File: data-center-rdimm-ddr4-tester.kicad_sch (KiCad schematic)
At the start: 13 parts, among them M1 1296.2013

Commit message: Exclude virtual components from bom
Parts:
- MP1, MP2, MP3, MP4, N1, N2: now left out of the parts list
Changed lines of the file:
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@@
   )
   (symbol (lib_id "data-center-rdimm-ddr4-tester:antmicro_logo") (at 165.735 281.305 0) (unit 1)
-    (in_bom yes) (on_board yes)
+    (in_bom no) (on_board yes)
     (property "Reference" "N2" (id 0) (at 171.1706 278.9428 0)
       (effects (font (size 1.27 1.27)) (justify left))
@@
   )
   (symbol (lib_id "data-center-rdimm-ddr4-tester:oshw_logo") (at 166.37 273.685 0) (unit 1)
-    (in_bom yes) (on_board yes)
+    (in_bom no) (on_board yes)
     (property "Reference" "N1" (id 0) (at 171.2976 273.6088 0)
       (effects (font (size 1.27 1.27)) (justify left))
@@
   )
   (symbol (lib_id "data-center-rdimm-ddr4-tester:PCB_Mount_Hole_3_NPTH") (at 88.9 279.4 0) (unit 1)
-    (in_bom yes) (on_board yes) (fields_autoplaced)
+    (in_bom no) (on_board yes) (fields_autoplaced)
     (property "Reference" "MP2" (id 0) (at 94.107 278.5653 0)
       (effects (font (size 1.27 1.27)) (justify left))
@@
   )
   (symbol (lib_id "data-center-rdimm-ddr4-tester:PCB_Mount_Hole_3_NPTH") (at 88.9 266.7 0) (unit 1)
-    (in_bom yes) (on_board yes) (fields_autoplaced)
+    (in_bom no) (on_board yes) (fields_autoplaced)
     (property "Reference" "MP1" (id 0) (at 94.107 265.8653 0)
       (effects (font (size 1.27 1.27)) (justify left))
@@
   )
   (symbol (lib_id "data-center-rdimm-ddr4-tester:PCB_Mount_Hole_3_NPTH") (at 127 279.4 0) (unit 1)
-    (in_bom yes) (on_board yes) (fields_autoplaced)
+    (in_bom no) (on_board yes) (fields_autoplaced)
     (property "Reference" "MP4" (id 0) (at 132.207 278.5653 0)
       (effects (font (size 1.27 1.27)) (justify left))
@@
   )
   (symbol (lib_id "data-center-rdimm-ddr4-tester:PCB_Mount_Hole_3_NPTH") (at 127 266.7 0) (unit 1)
-    (in_bom yes) (on_board yes) (fields_autoplaced)
+    (in_bom no) (on_board yes) (fields_autoplaced)
     (property "Reference" "MP3" (id 0) (at 132.207 265.8653 0)
       (effects (font (size 1.27 1.27)) (justify left))

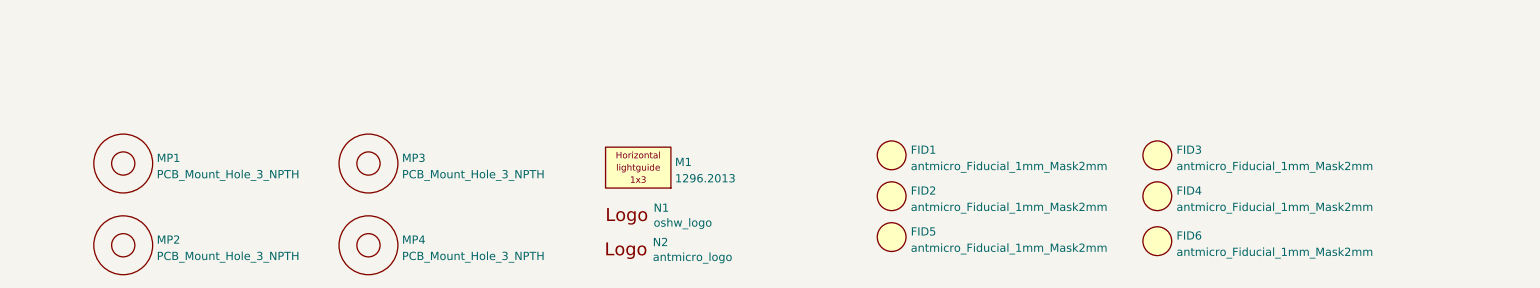
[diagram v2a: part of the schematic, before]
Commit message: Introduce component standardization
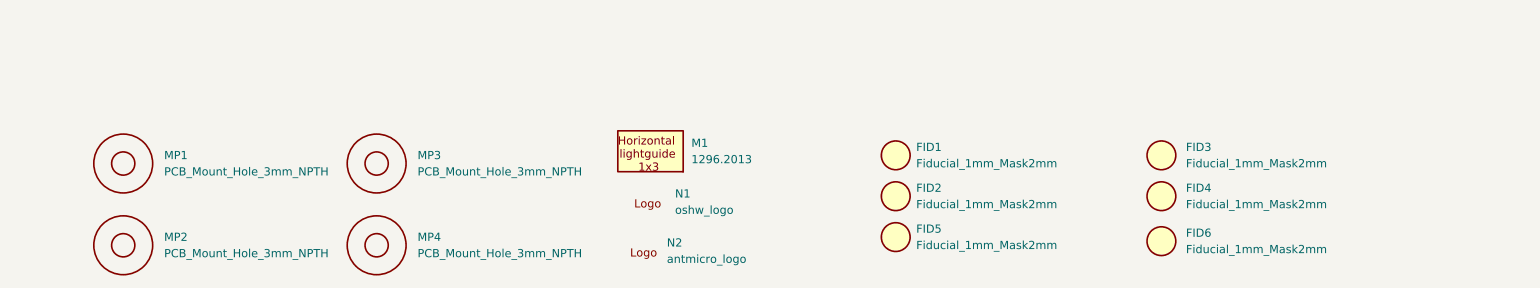
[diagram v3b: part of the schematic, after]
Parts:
- FID1, FID2, FID3, FID4, FID5, FID6: value antmicro_Fiducial_1mm_Mask2mm -> Fiducial_1mm_Mask2mm; symbol data-center-rdimm-ddr4-tester:antmicro_Fiducial_1mm_Mask2mm -> data-center-rdimm-ddr4-tester:Fiducial_1mm_Mask2mm; Author (none) -> Antmicro; License (none) -> Apache-2.0
- M1: value 1296.2013 -> Mech_Lightpipe_Mentor_1296.2013; footprint data-center-rdimm-ddr4-tester-footprints:Mentor_1296.2013 -> data-center-rdimm-ddr4-tester-footprints:Mech_Lightpipe_Mentor_1296.2013; symbol data-center-rdimm-ddr4-tester:1296.2013 -> data-center-rdimm-ddr4-tester:Mech_Lightpipe_Mentor_1296.2013; Author (none) -> Antmicro; License (none) -> Apache-2.0
- MP1, MP2, MP3, MP4: value PCB_Mount_Hole_3_NPTH -> PCB_Mount_Hole_3mm_NPTH; symbol data-center-rdimm-ddr4-tester:PCB_Mount_Hole_3_NPTH -> data-center-rdimm-ddr4-tester:PCB_Mount_Hole_3mm_NPTH; Author (none) -> Antmicro; License (none) -> Apache-2.0; now in the parts list
- N1: footprint data-center-rdimm-ddr4-tester-footprints:OSHW-Logo_5.7x6mm_Mask -> data-center-rdimm-ddr4-tester-footprints:oshw-logo; Author (none) -> Antmicro; License (none) -> Apache-2.0; now in the parts list
- N2: Author (none) -> Antmicro; License (none) -> Apache-2.0; now in the parts list
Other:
- moved on the sheet: FID1, FID2, FID3, FID4, FID5, FID6, M1, MP3, MP4, N1, N2

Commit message: [#55119] component update
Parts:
- FID1, FID2, FID3, FID4, FID5, FID6: footprint data-center-rdimm-ddr4-tester-footprints:Fiducial_1mm_Mask2mm -> antmicro-footprints:Fiducial_1mm_Mask2mm; symbol data-center-rdimm-ddr4-tester:Fiducial_1mm_Mask2mm -> antmicroFiducialMarks:Fiducial_1mm_Mask2mm
- N1: footprint data-center-rdimm-ddr4-tester-footprints:oshw-logo -> antmicro-footprints:oshw-logo; symbol data-center-rdimm-ddr4-tester:oshw_logo -> antmicroMechanicalParts:oshw_logo
- N2: footprint data-center-rdimm-ddr4-tester-footprints:antmicro-logo_scaled_20mm_mask -> antmicro-footprints:antmicro-logo; symbol data-center-rdimm-ddr4-tester:antmicro_logo -> antmicroMechanicalParts:antmicro_logo
